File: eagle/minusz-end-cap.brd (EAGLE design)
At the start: 106 x 106 mm, 28 parts, among them U1 TCA9543A-PW, U3 HMC5883L, U4 HMC5883L

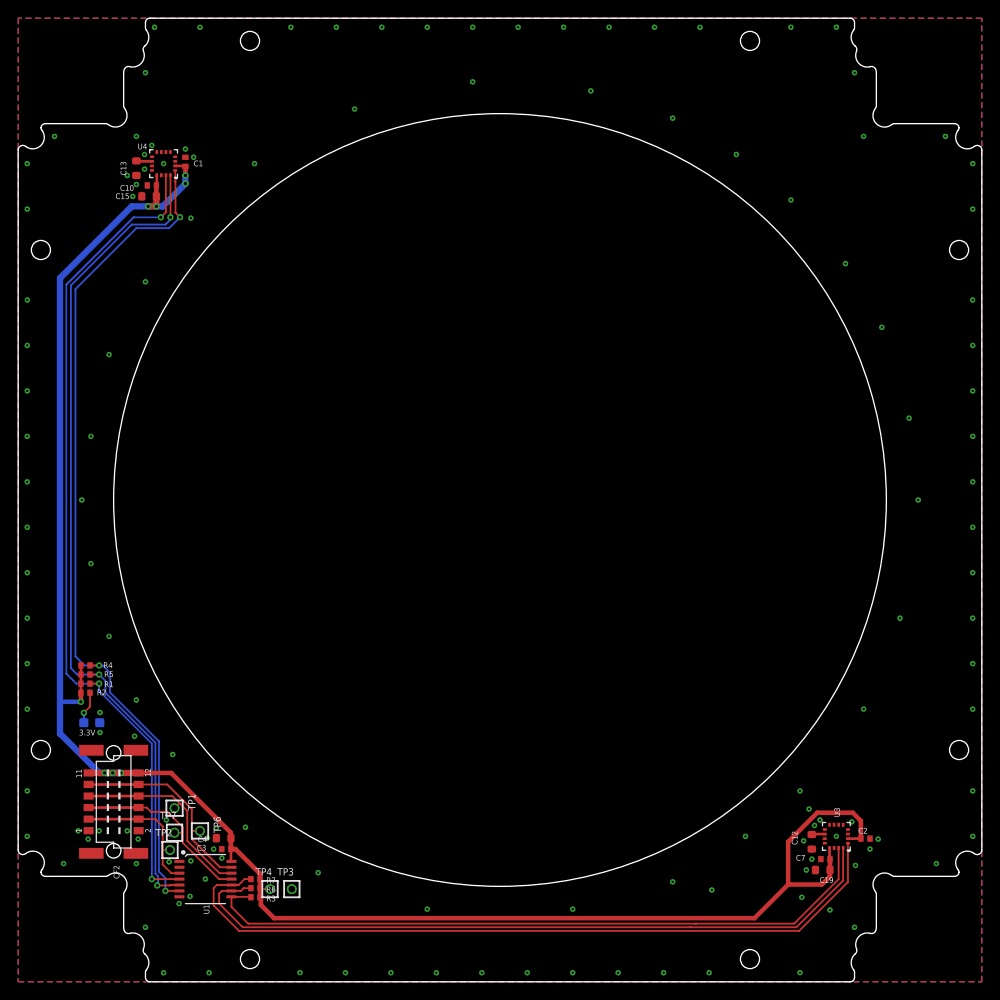
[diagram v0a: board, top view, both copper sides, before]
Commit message: Added debug cutout to -Z end cap, and fixed README.
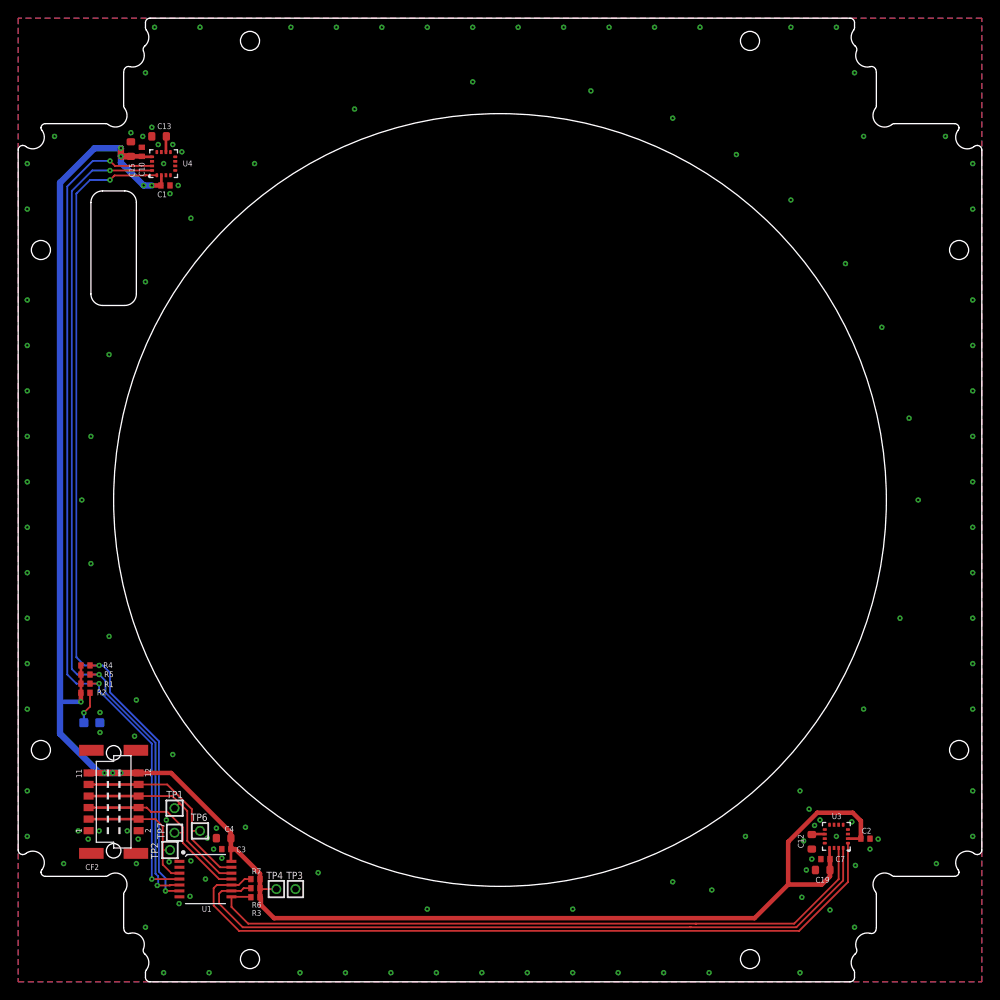
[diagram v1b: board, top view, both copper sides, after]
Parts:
- moved C15 5.57 mm to (12.4, 91.6), turned to 90 degrees
- moved C13 4.30 mm to (15.5, 93.0), turned to 180 degrees
- moved C10 3.86 mm to (13.6, 91.3), turned to 90 degrees
- moved C1 3.41 mm to (16.2, 87.6), turned to 0 degrees
- moved TP4 0.70 mm to (28.4, 10.2)
- moved TP3 0.40 mm to (30.5, 10.2)
- turned U4 to 90 degrees
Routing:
- net 3.3V: track 206.9 -> 213.4 mm
- net !INT0: track 93.1 -> 96.3 mm
- net SDA0: track 93.7 -> 95.0 mm
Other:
- outline, holes or cut-outs redrawn
- board text removed: "3.3V"
